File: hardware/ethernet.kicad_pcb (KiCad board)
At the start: 2 copper layers, 24 x 45.4 mm, 3 parts, among them J1 Conn_02x03_Odd_Even, J2 Conn_01x16, J3 Conn_01x12

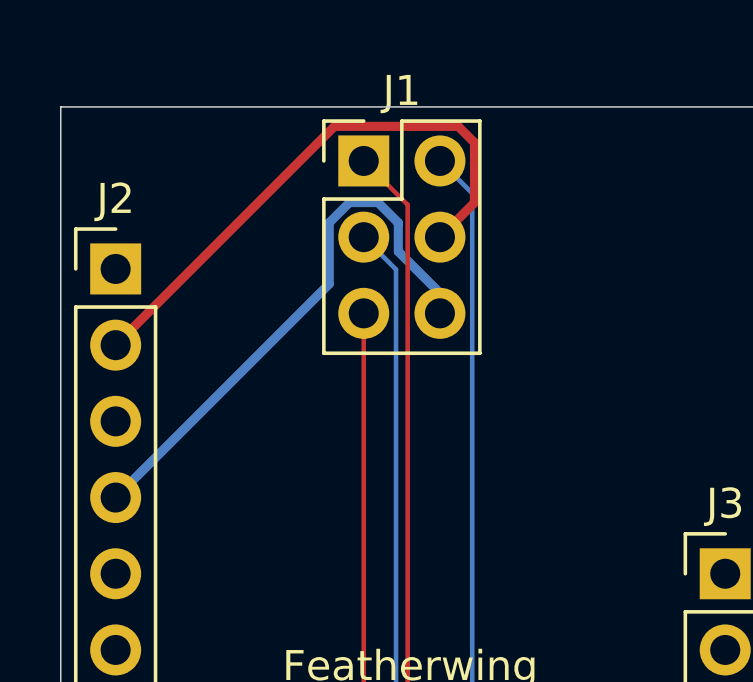
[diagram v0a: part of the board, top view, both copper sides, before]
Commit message: Correct placement of bottom-facing header on Ethernet adapter board
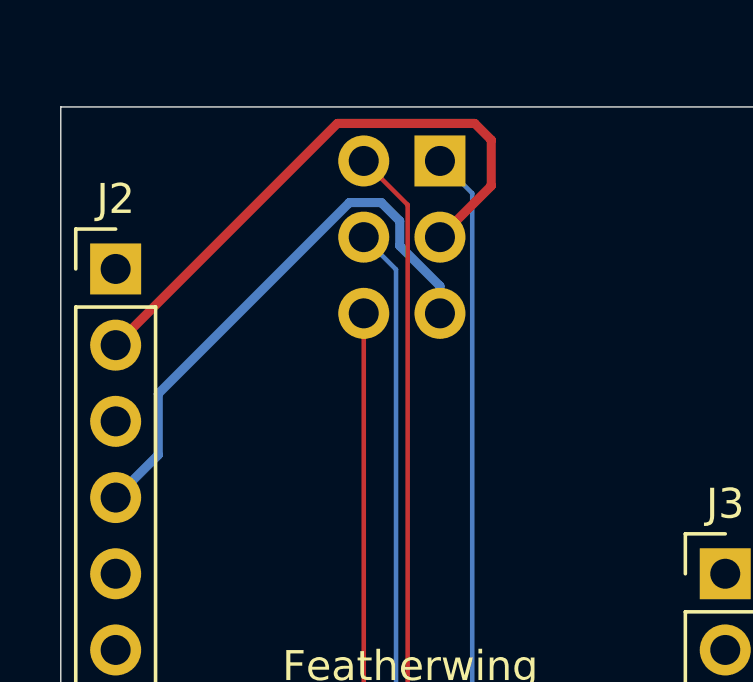
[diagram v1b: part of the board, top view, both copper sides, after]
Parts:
- J1: moved to B.Cu
- moved J1 2.54 mm to (27.2, 18.3), turned to 180 degrees
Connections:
- J1 pad 1: /MOSI -> /~{CS}
- J1 pad 2: /~{CS} -> /MOSI
- J1 pad 3: /MISO -> +3.3V
- J1 pad 4: +3.3V -> /MISO
- J1 pad 5: /SCK -> GND
- J1 pad 6: GND -> /SCK
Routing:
- net +3.3V: track 18.8 -> 19.8 mm
